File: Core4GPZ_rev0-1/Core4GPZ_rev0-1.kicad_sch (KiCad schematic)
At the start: 3 parts, among them U1 core4, U2 MPX4250

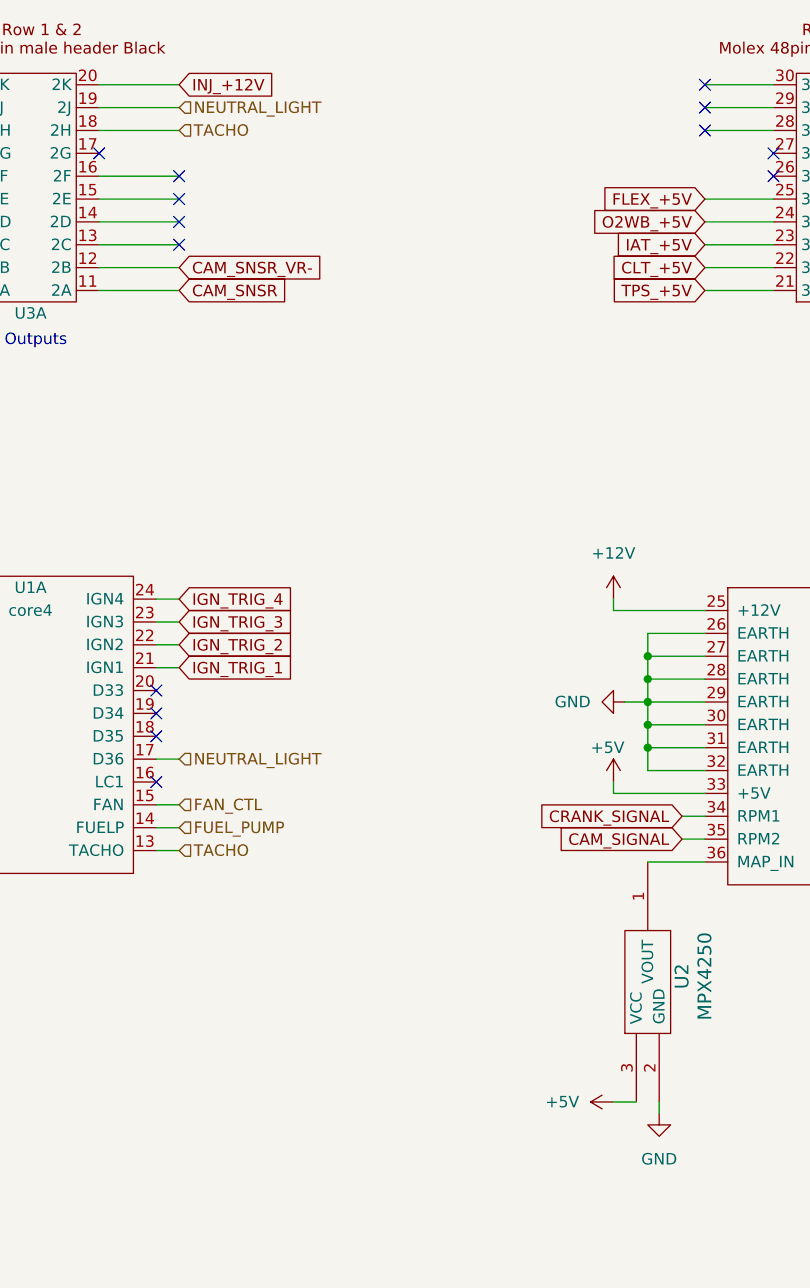
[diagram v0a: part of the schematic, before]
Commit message: Frist revision
First revision finished, optimised routing, board turned 180°.
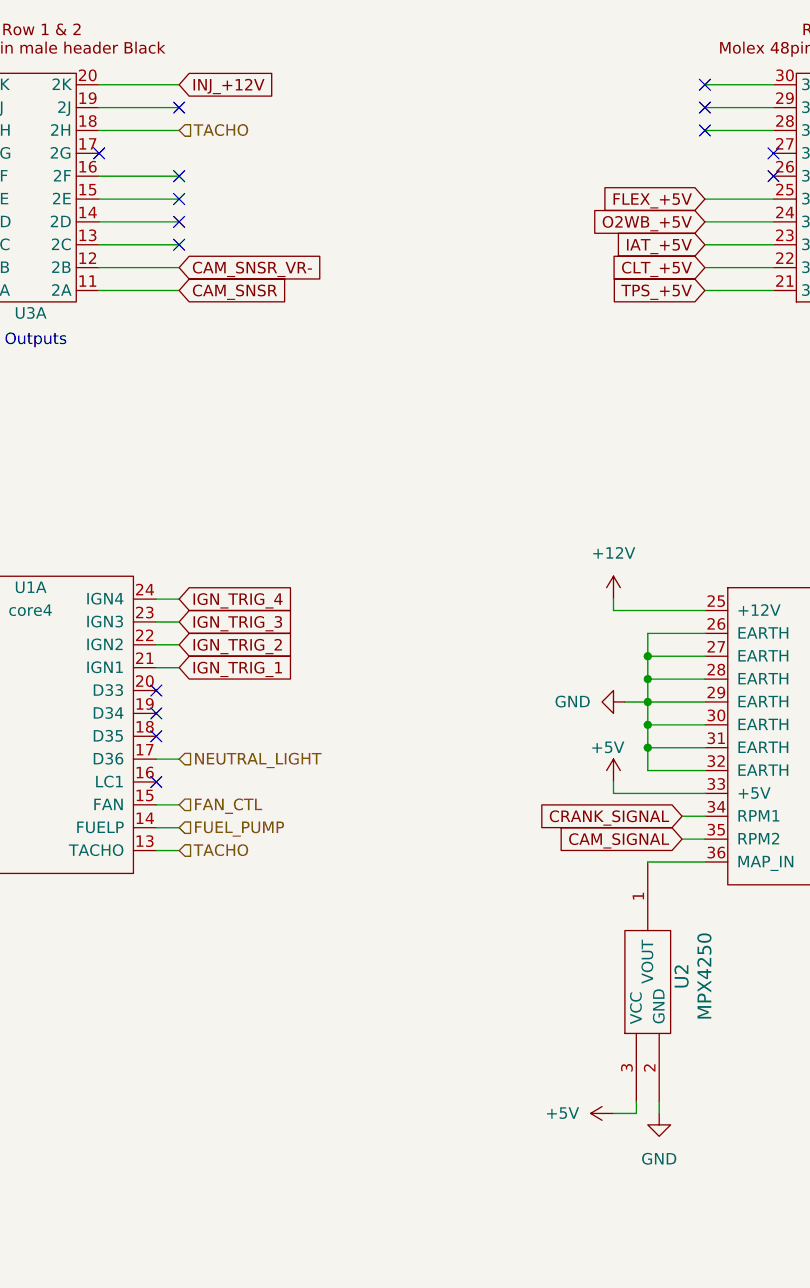
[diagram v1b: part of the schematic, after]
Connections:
- net NEUTRAL_LIGHT: no longer U3.19 (2J)
- no-connect marks 40 -> 41
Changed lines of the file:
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@@
+	)
+	(no_connect
+		(at 85.09 31.75)
 	)
 	(no_connect
@@
 	(wire
 		(pts
+			(xy 135.89 143.51) (xy 135.89 142.24)
+		)
+		(stroke
+			(width 0)
+			(type default)
+		)
+	)
+	(wire
+		(pts
 			(xy 143.51 49.53) (xy 151.13 49.53)
 		)
@@
 	(wire
 		(pts
-			(xy 133.35 142.24) (xy 135.89 142.24)
+			(xy 133.35 143.51) (xy 135.89 143.51)
 		)
 		(stroke
@@
 		(shape input)
 		(at 175.26 49.53 0)
-		(fields_autoplaced yes)
-		(effects
-			(font
-				(size 1.27 1.27)
-			)
-			(justify left)
-		)
-	)
-	(hierarchical_label "NEUTRAL_LIGHT"
-		(shape input)
-		(at 85.09 31.75 0)
 		(fields_autoplaced yes)
 		(effects
@@
 	(symbol
 		(lib_id "power:+5V")
-		(at 133.35 142.24 90)
+		(at 133.35 143.51 90)
 		(unit 1)
 		(exclude_from_sim no)
@@
 		(fields_autoplaced yes)
 		(property "Reference" "#PWR07"
-			(at 137.16 142.24 0)
+			(at 137.16 143.51 0)
 			(effects
 				(font
@@
 		)
 		(property "Value" "+5V"
-			(at 129.54 142.24 90)
+			(at 129.54 143.51 90)
 			(effects
 				(font
@@
 		)
 		(property "Footprint" ""
-			(at 133.35 142.24 0)
+			(at 133.35 143.51 0)
 			(effects
 				(font
@@
 		)
 		(property "Datasheet" ""
-			(at 133.35 142.24 0)
+			(at 133.35 143.51 0)
 			(effects
 				(font
@@
 		)
 		(property "Description" ""
-			(at 133.35 142.24 0)
-			(effects
-				(font
+			(at 133.35 143.51 0)
+			(effects
+				(font

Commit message: Rewied ground plane, set all SNSR+5V ref to one pin
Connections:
- net CLT_+5V: no longer names the net of U3.22 (3B)
- net FLEX_+5V: no longer names the net of U3.25 (3E)
- net IAT_+5V: no longer names the net of U3.23 (3C)
- net O2WB_+5V: no longer names the net of U3.24 (3D)
- net TPS_+5V renamed SNSR_+5V
- no-connect marks 41 -> 45
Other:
- moved on the sheet: U1C, U3C

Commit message: Added informations for Molex CMC conn
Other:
- note added: "500762-0481"
- note added: "Note for Molex CMC48Way Connector : Male part (PCB Header) : 500762-0481 Female part : 64320-3311 0.635mm CMC CP Female Terminals : 64322 1.5mm CMC CP Female Terminals : 64323"
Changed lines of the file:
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@@
+		)
+	)
+	(text "500762-0481"
+		(exclude_from_sim no)
+		(at 246.38 20.32 0)
+		(effects
+			(font
+				(size 1.27 1.27)
+			)
 		)
 	)
@@
 		)
 	)
+	(text "500762-0481"
+		(exclude_from_sim no)
+		(at 158.75 19.812 0)
+		(effects
+			(font
+				(size 1.27 1.27)
+			)
+		)
+	)
+	(text "500762-0481"
+		(exclude_from_sim no)
+		(at 69.088 20.574 0)
+		(effects
+			(font
+				(size 1.27 1.27)
+			)
+		)
+	)
+	(text "Note for Molex CMC48Way Connector :\nMale part (PCB Header) : 500762-0481\nFemale part : 64320-3311\n0.635mm CMC CP Female Terminals : 64322\n1.5mm CMC CP Female Terminals : 64323"
+		(exclude_from_sim no)
+		(at 249.936 61.214 0)
+		(effects
+			(font
+				(size 1.27 1.27)
+			)
+		)
+	)

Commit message: Reworked the VR conditionner
Schematic and PCB based on the Dropbear model
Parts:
- renumbered U3 to U1, U1 to U2, U2 to U3
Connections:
- net BIKE_+12V_SWITCHED_IN: now also U1.42 (1M)
- net BIKE_GROUND: no longer U1.42 (1M)
- net CAM_SNSR: now also U1.1 (1A); no longer U1.11 (2A)
- net CAM_SNSR_VR-: now also U1.2 (1B); no longer U1.12 (2B)
- net CRANK_SNSR: now also U1.11 (2A); no longer U1.1 (1A)
- net CRANK_SNSR_VR-: now also U1.12 (2B); no longer U1.2 (1B)
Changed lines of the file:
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@@
 	)
 	(junction
-		(at 236.22 41.91)
+		(at 137.16 92.71)
 		(diameter 0)
 		(color 0 0 0 0)
 	)
 	(junction
-		(at 137.16 92.71)
+		(at 236.22 34.29)
 		(diameter 0)
 		(color 0 0 0 0)
@@
 	(wire
 		(pts
-			(xy 238.76 34.29) (xy 232.41 34.29)
+			(xy 238.76 34.29) (xy 236.22 34.29)
 		)
 		(stroke
@@
 	(wire
 		(pts
+			(xy 238.76 36.83) (xy 236.22 36.83)
+		)
+		(stroke
+			(width 0)
+			(type default)
+		)
+	)
+	(wire
+		(pts
 			(xy 172.72 95.25) (xy 175.26 95.25)
 		)
@@
 	(wire
 		(pts
-			(xy 236.22 36.83) (xy 236.22 41.91)
-		)
-		(stroke
-			(width 0)
-			(type default)
-		)
-	)
-	(wire
-		(pts
 			(xy 166.37 49.53) (xy 175.26 49.53)
 		)
@@
 	(wire
 		(pts
+			(xy 236.22 34.29) (xy 232.41 34.29)
+		)
+		(stroke
+			(width 0)
+			(type default)
+		)
+	)
+	(wire
+		(pts
 			(xy 129.54 86.36) (xy 129.54 87.63)
 		)
@@
 	(wire
 		(pts
-			(xy 76.2 34.29) (xy 85.09 34.29)
+			(xy 236.22 36.83) (xy 236.22 34.29)
 		)
 		(stroke
@@
 	(wire
 		(pts
-			(xy 137.16 95.25) (xy 137.16 97.79)
+			(xy 76.2 34.29) (xy 85.09 34.29)
 		)
 		(stroke
@@
 	(wire
 		(pts
-			(xy 166.37 52.07) (xy 175.26 52.07)
+			(xy 137.16 95.25) (xy 137.16 97.79)
 		)
 		(stroke
@@
 	(wire
 		(pts
-			(xy 143.51 90.17) (xy 137.16 90.17)
+			(xy 166.37 52.07) (xy 175.26 52.07)
 		)
 		(stroke
@@
 	(wire
 		(pts
-			(xy 82.55 88.9) (xy 85.09 88.9)
+			(xy 143.51 90.17) (xy 137.16 90.17)
 		)
 		(stroke
@@
 	(wire
 		(pts
-			(xy 82.55 86.36) (xy 85.09 86.36)
+			(xy 82.55 88.9) (xy 85.09 88.9)
 		)
 		(stroke
@@
 	(wire
 		(pts
-			(xy 236.22 36.83) (xy 238.76 36.83)
+			(xy 82.55 86.36) (xy 85.09 86.36)
 		)
 		(stroke
@@
 	(global_label "CRANK_SNSR_VR-"
 		(shape input)
-		(at 54.61 49.53 180)
+		(at 85.09 49.53 0)
 		(fields_autoplaced yes)
 		(effects
@@
 				(size 1.27 1.27)
 			)
-			(justify right)
+			(justify left)
 		)
 		(property "Intersheetrefs" "${INTERSHEET_REFS}"
-			(at 34.51 49.53 0)
+			(at 105.19 49.53 0)
 			(effects
 				(font
 					(size 1.27 1.27)
 				)
-				(justify right)
+				(justify left)
 				(hide yes)
 			)
@@
 	(global_label "CAM_SNSR"
 		(shape input)
-		(at 85.09 52.07 0)
+		(at 54.61 52.07 180)
 		(fields_autoplaced yes)
 		(effects
@@
 				(size 1.27 1.27)
 			)
-			(justify left)
+			(justify right)
 		)
 		(property "Intersheetrefs" "${INTERSHEET_REFS}"
-			(at 97.8723 52.07 0)
+			(at 41.8277 52.07 0)
 			(effects
 				(font
 					(size 1.27 1.27)
 				)
-				(justify left)
+				(justify right)
 				(hide yes)
 			)
@@
 	(global_label "CAM_SNSR_VR-"
 		(shape input)
-		(at 85.09 49.53 0)
+		(at 54.61 49.53 180)
 		(fields_autoplaced yes)
 		(effects
@@
 				(size 1.27 1.27)
 			)
-			(justify left)
+			(justify right)
 		)
 		(property "Intersheetrefs" "${INTERSHEET_REFS}"
-			(at 102.7709 49.53 0)
+			(at 36.9291 49.53 0)
 			(effects
 				(font
 					(size 1.27 1.27)
 				)
-				(justify left)
+				(justify right)
 				(hide yes)
 			)
@@
 	(global_label "CRANK_SNSR"
 		(shape input)
-		(at 54.61 52.07 180)
+		(at 85.09 52.07 0)
 		(fields_autoplaced yes)
 		(effects
@@
 				(size 1.27 1.27)
 			)
-			(justify right)
+			(justify left)
 		)
 		(property "Intersheetrefs" "${INTERSHEET_REFS}"
-			(at 39.4086 52.07 0)
+			(at 100.2914 52.07 0)
 			(effects
 				(font
 					(size 1.27 1.27)
 				)
-				(justify right)
+				(justify left)
 				(hide yes)
 			)
@@
 		(on_board yes)
 		(dnp no)
-		(property "Reference" "U1"
+		(property "Reference" "U2"
 			(at 158.75 86.36 0)
 			(effects
@@
 			(project "Core4GPZ_rev0-1"
 				(path "/ac28f42d-34b3-4fcc-84dd-ab6106f99610"
-					(reference "U1")
+					(reference "U2")
 					(unit 2)
 				)
@@
 		(dnp no)
 		(fields_autoplaced yes)
-		(property "Reference" "#PWR06"
+		(property "Reference" "#PWR05"
 			(at 138.43 149.86 0)
 			(effects
@@
 			(project "Core4GPZ_rev0-1"
 				(path "/ac28f42d-34b3-4fcc-84dd-ab6106f99610"
-					(reference "#PWR06")
+					(reference "#PWR05")
 					(unit 1)
 				)
@@
 		(on_board yes)
 		(dnp no)
-		(property "Reference" "U1"
+		(property "Reference" "U2"
 			(at 68.58 85.09 0)
 			(effects
@@
 			(project "Core4GPZ_rev0-1"
 				(path "/ac28f42d-34b3-4fcc-84dd-ab6106f99610"
-					(reference "U1")
+					(reference "U2")
 					(unit 1)
 				)
@@
 		(on_board yes)
 		(dnp no)
-		(property "Reference" "U3"
+		(property "Reference" "U1"
 			(at 158.75 54.61 0)
 			(effects
@@
 			(project "Core4GPZ_rev0-1"
 				(path "/ac28f42d-34b3-4fcc-84dd-ab6106f99610"
-					(reference "U3")
+					(reference "U1")
 					(unit 2)
 				)
@@
 		(dnp no)
 		(fields_autoplaced yes)
-		(property "Reference" "#PWR011"
+		(property "Reference" "#PWR04"
 			(at 128.27 97.79 0)
 			(effects
@@
 			(project "Core4GPZ_rev0-1"
 				(path "/ac28f42d-34b3-4fcc-84dd-ab6106f99610"
-					(reference "#PWR011")
+					(reference "#PWR04")
 					(unit 1)
 				)
@@
 		(on_board yes)
 		(dnp no)
-		(property "Reference" "#PWR01"
+		(property "Reference" "#PWR02"
 			(at 129.54 110.49 0)
 			(effects
@@
 			(project "Core4GPZ_rev0-1"
 				(path "/ac28f42d-34b3-4fcc-84dd-ab6106f99610"
-					(reference "#PWR01")
+					(reference "#PWR02")
 					(unit 1)
 				)
@@
 		(on_board yes)
 		(dnp no)
-		(property "Reference" "U2"
+		(property "Reference" "U3"
 			(at 140.97 128.27 0)
 			(effects
@@
 			(project "Core4GPZ_rev0-1"
 				(path "/ac28f42d-34b3-4fcc-84dd-ab6106f99610"
-					(reference "U2")
+					(reference "U3")
 					(unit 1)
 				)
@@
 		(dnp no)
 		(fields_autoplaced yes)
-		(property "Reference" "#PWR04"
+		(property "Reference" "#PWR01"
 			(at 129.54 90.17 0)
 			(effects
@@
 			(project "Core4GPZ_rev0-1"
 				(path "/ac28f42d-34b3-4fcc-84dd-ab6106f99610"
-					(reference "#PWR04")
+					(reference "#PWR01")
 					(unit 1)
 				)
@@
 		(dnp no)
 		(fields_autoplaced yes)
-		(property "Reference" "#PWR07"
+		(property "Reference" "#PWR03"
 			(at 137.16 143.51 0)
 			(effects
@@
 			(project "Core4GPZ_rev0-1"
 				(path "/ac28f42d-34b3-4fcc-84dd-ab6106f99610"
-					(reference "#PWR07")
+					(reference "#PWR03")
 					(unit 1)
 				)
@@
 		(on_board yes)
 		(dnp no)
-		(property "Reference" "U3"
+		(property "Reference" "U1"
 			(at 68.58 54.61 0)
 			(effects
@@
 			(project "Core4GPZ_rev0-1"
 				(path "/ac28f42d-34b3-4fcc-84dd-ab6106f99610"
-					(reference "U3")
+					(reference "U1")
 					(unit 1)
 				)
@@
 		(dnp no)
 		(fields_autoplaced yes)
-		(property "Reference" "U3"
+		(property "Reference" "U1"
 			(at 246.38 25.4 0)
 			(effects
@@
 			(project "Core4GPZ_rev0-1"
 				(path "/ac28f42d-34b3-4fcc-84dd-ab6106f99610"
-					(reference "U3")
+					(reference "U1")
 					(unit 3)
 				)
@@
 		(on_board yes)
 		(dnp no)
-		(property "Reference" "U1"
+		(property "Reference" "U2"
 			(at 246.38 96.52 0)
 			(effects
@@
 			(project "Core4GPZ_rev0-1"
 				(path "/ac28f42d-34b3-4fcc-84dd-ab6106f99610"
-					(reference "U1")
+					(reference "U2")
 					(unit 3)
 				)
@@
 		(dnp no)
 		(fields_autoplaced yes)
-		(property "Reference" "#PWR012"
+		(property "Reference" "#PWR06"
 			(at 222.25 109.22 0)
 			(effects
@@
 			(project "Core4GPZ_rev0-1"
 				(path "/ac28f42d-34b3-4fcc-84dd-ab6106f99610"
-					(reference "#PWR012")
+					(reference "#PWR06")
 					(unit 1)
 				)

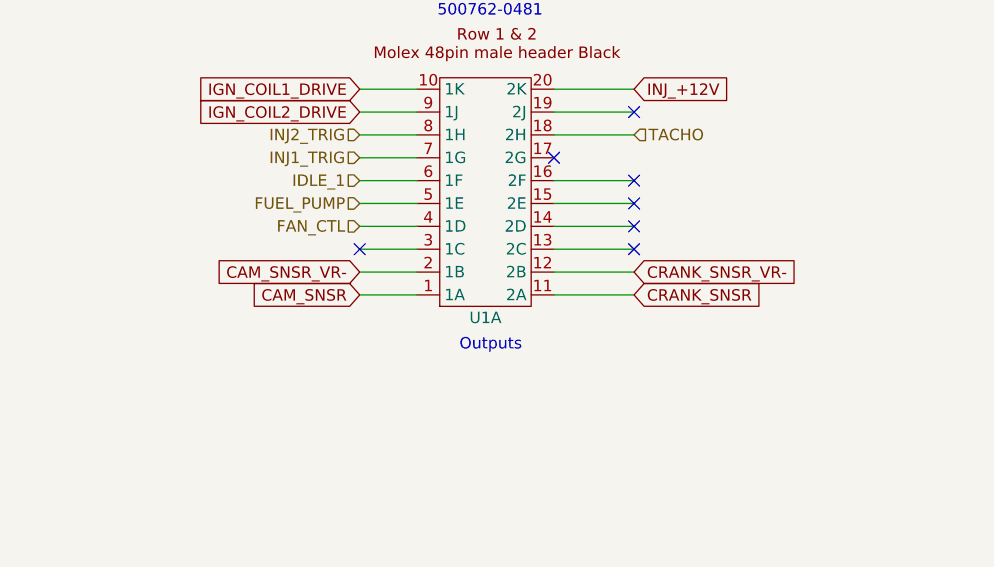
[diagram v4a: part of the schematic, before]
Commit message: Moved VR Conditionner.
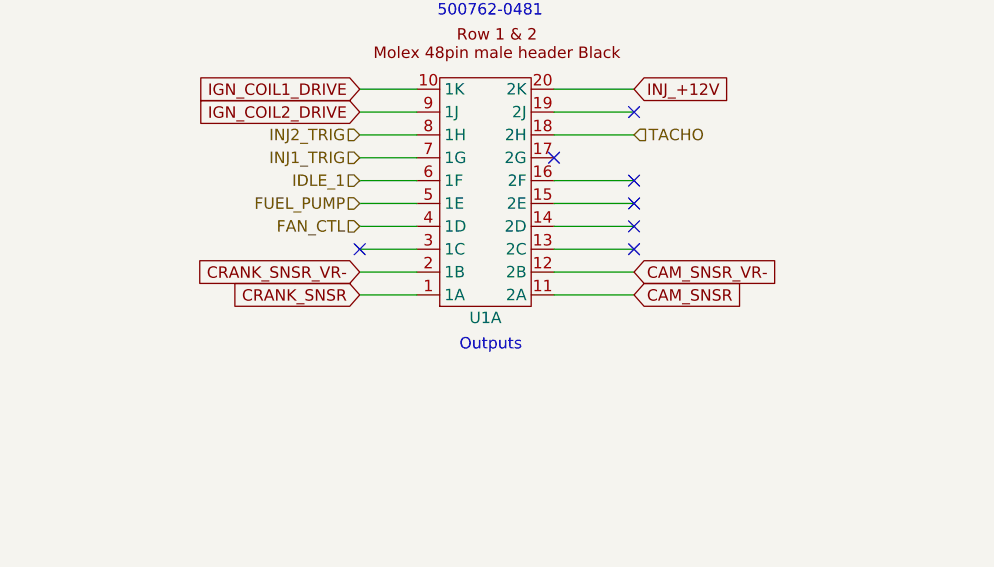
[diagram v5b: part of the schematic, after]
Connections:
- net CAM_SNSR: now also U1.11 (2A); no longer U1.1 (1A)
- net CAM_SNSR_VR-: now also U1.12 (2B); no longer U1.2 (1B)
- net CRANK_SNSR: now also U1.1 (1A); no longer U1.11 (2A)
- net CRANK_SNSR_VR-: now also U1.2 (1B); no longer U1.12 (2B)
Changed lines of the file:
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@@
 	(global_label "CRANK_SNSR_VR-"
 		(shape input)
-		(at 85.09 49.53 0)
+		(at 54.61 49.53 180)
 		(fields_autoplaced yes)
 		(effects
@@
 				(size 1.27 1.27)
 			)
-			(justify left)
+			(justify right)
 		)
 		(property "Intersheetrefs" "${INTERSHEET_REFS}"
-			(at 105.19 49.53 0)
+			(at 34.51 49.53 0)
 			(effects
 				(font
 					(size 1.27 1.27)
 				)
-				(justify left)
+				(justify right)
 				(hide yes)
 			)
@@
 	(global_label "CAM_SNSR"
 		(shape input)
-		(at 54.61 52.07 180)
+		(at 85.09 52.07 0)
 		(fields_autoplaced yes)
 		(effects
@@
 				(size 1.27 1.27)
 			)
-			(justify right)
+			(justify left)
 		)
 		(property "Intersheetrefs" "${INTERSHEET_REFS}"
-			(at 41.8277 52.07 0)
+			(at 97.8723 52.07 0)
 			(effects
 				(font
 					(size 1.27 1.27)
 				)
-				(justify right)
+				(justify left)
 				(hide yes)
 			)
@@
 	(global_label "CAM_SNSR_VR-"
 		(shape input)
-		(at 54.61 49.53 180)
+		(at 85.09 49.53 0)
+		(fields_autoplaced yes)
+		(effects
+			(font
+				(size 1.27 1.27)
+			)
+			(justify left)
+		)
+		(property "Intersheetrefs" "${INTERSHEET_REFS}"
+			(at 102.7709 49.53 0)
+			(effects
+				(font
+					(size 1.27 1.27)
+				)
+				(justify left)
+				(hide yes)
+			)
+		)
+	)
+	(global_label "CRANK_SNSR"
+		(shape input)
+		(at 54.61 52.07 180)
 		(fields_autoplaced yes)
 		(effects
@@
 		)
 		(property "Intersheetrefs" "${INTERSHEET_REFS}"
-			(at 36.9291 49.53 0)
+			(at 39.4086 52.07 0)
 			(effects
 				(font
@@
 				(hide yes)
 			)
-		)
-	)
-	(global_label "CRANK_SNSR"
-		(shape input)
-		(at 85.09 52.07 0)
-		(fields_autoplaced yes)
-		(effects
-			(font
-				(size 1.27 1.27)
-			)
-			(justify left)
-		)
-		(property "Intersheetrefs" "${INTERSHEET_REFS}"
-			(at 100.2914 52.07 0)
-			(effects
-				(font
-					(size 1.27 1.27)
-				)
-				(justify left)
-				(hide yes)
-			)
